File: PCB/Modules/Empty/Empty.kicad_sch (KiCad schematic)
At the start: 3 parts

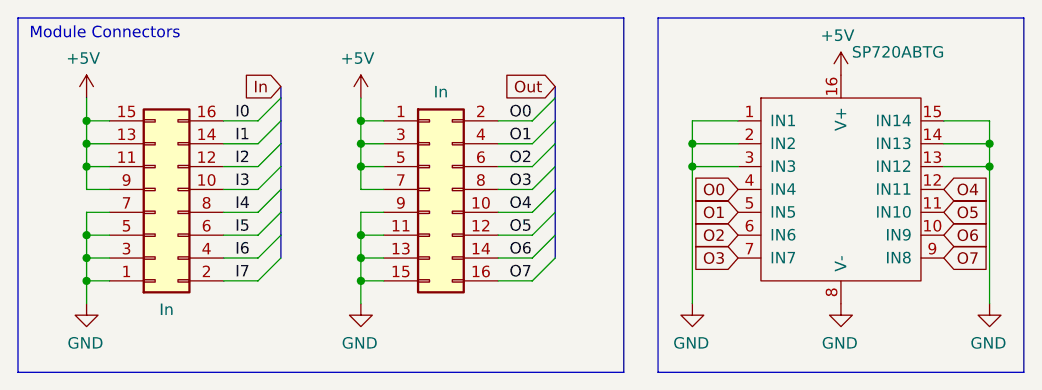
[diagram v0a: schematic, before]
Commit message: Upgrade KiCad files from 6.0 to 7.0.
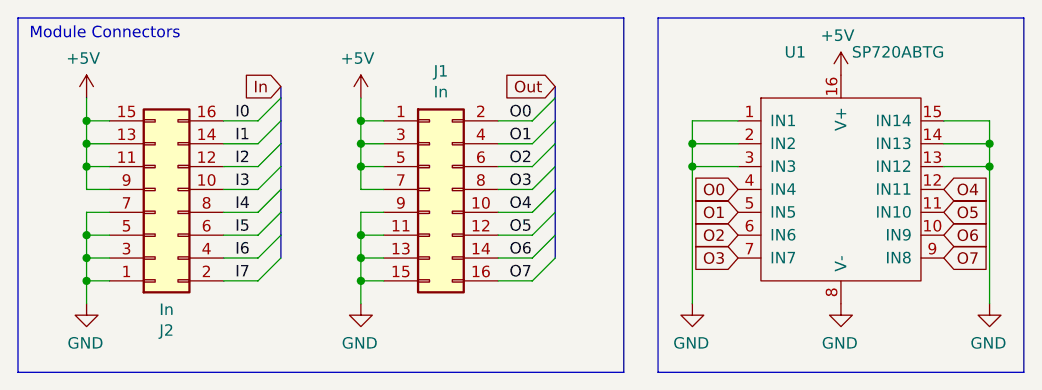
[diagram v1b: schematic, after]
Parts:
- gave numbers to parts that had none: 3
